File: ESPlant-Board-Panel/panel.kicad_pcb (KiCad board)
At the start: 4 copper layers, 70 x 116 mm, 150 parts, among them J1 Conn_01x05, U1 USB-C, U13 ESP32-C6-MINI-1-N4, U3 AHT20-F, U4 Tactile-Switch, U5 3.3V-Regulator, U6 Light sensor, U7 Tactile-Switch, U8 Slide-Switch, U9 Battery-Spring

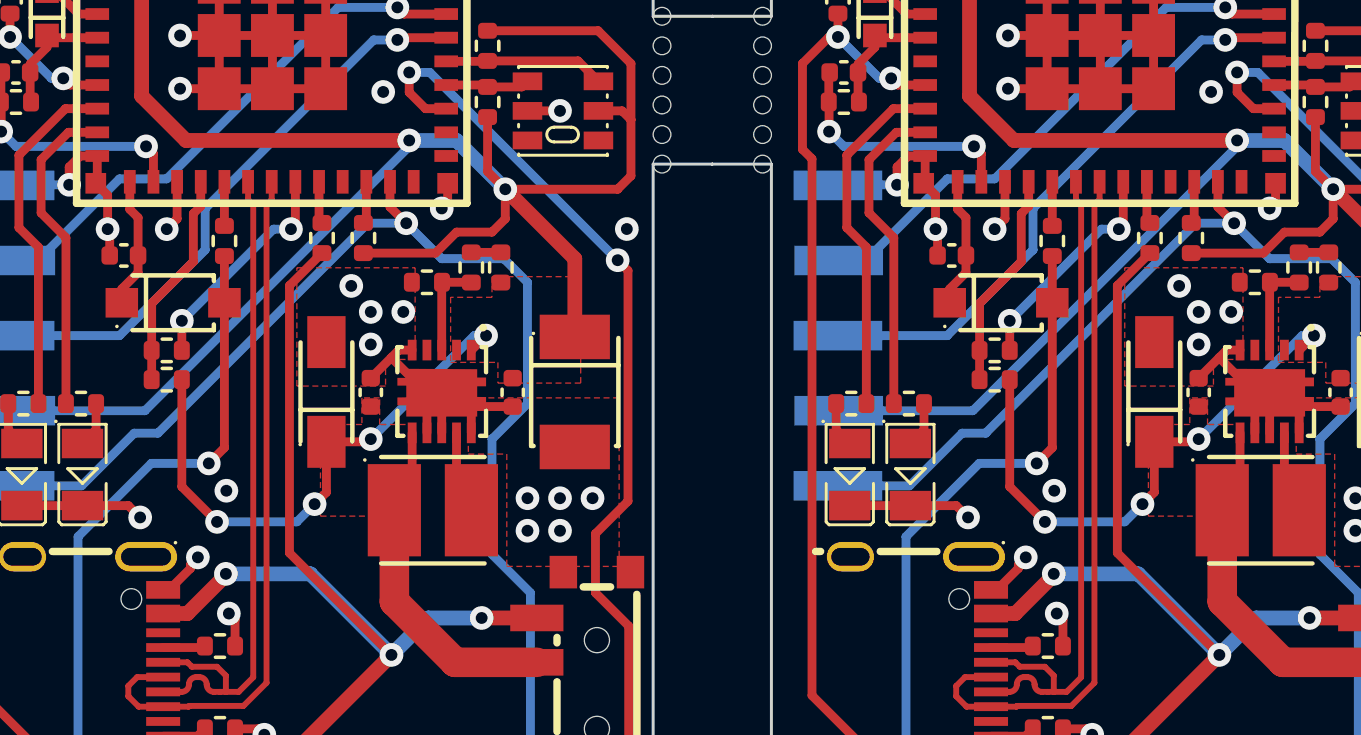
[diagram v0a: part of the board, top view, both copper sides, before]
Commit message: Panel: Add voltage divider for checking usb connection
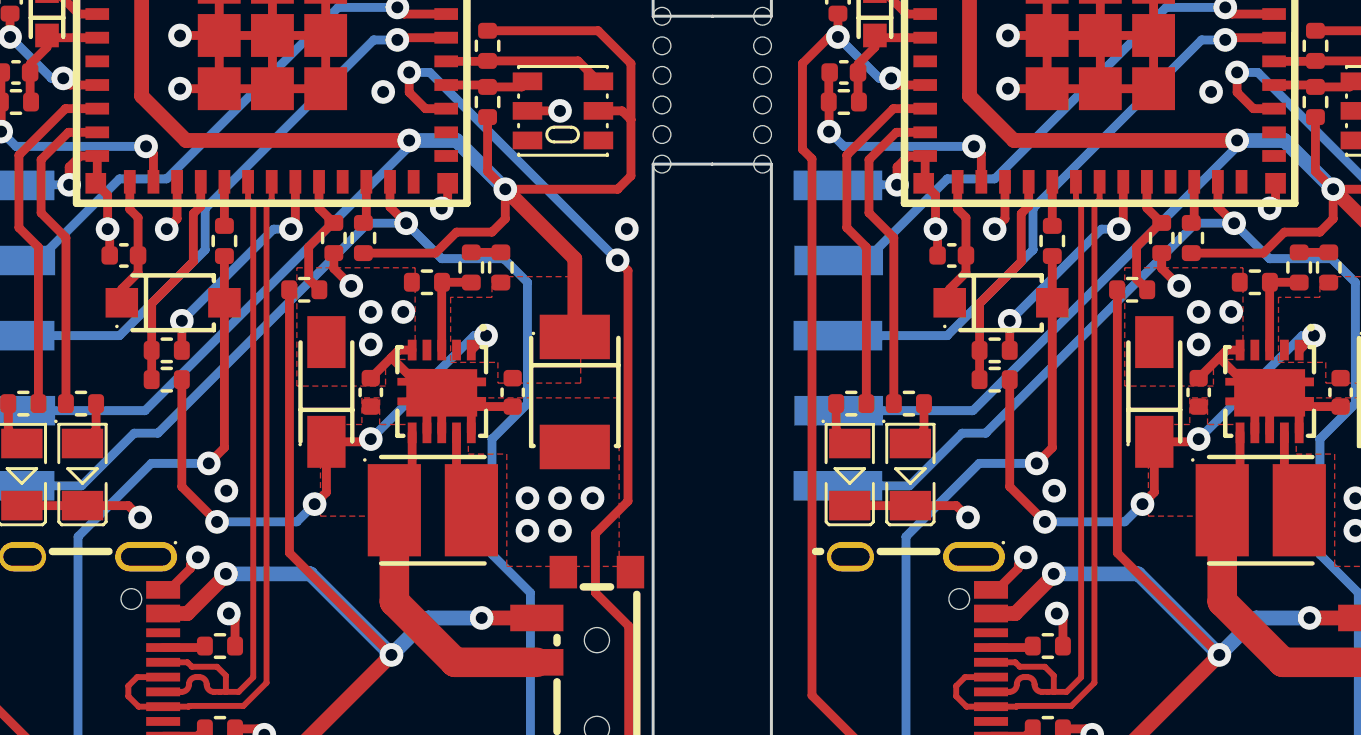
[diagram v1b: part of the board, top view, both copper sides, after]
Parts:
- removed the R7 at (239.8, 32.5)
- removed the R7 at (211.8, 32.5)
- added R17: 20k, Resistor_SMD:R_0402_1005Metric, F.Cu at (240.2, 32.5)
- added R17: 20k, Resistor_SMD:R_0402_1005Metric, F.Cu at (212.2, 32.5)
- added R7: 10k, Resistor_SMD:R_0402_1005Metric, F.Cu at (211.2, 34.2)
- added R7: 10k, Resistor_SMD:R_0402_1005Metric, F.Cu at (239.2, 34.2)
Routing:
- net Board_1-Net-(U13-IO15): track 1.43 -> 4.38 mm
- net Board_0-Net-(U13-IO15): track 1.43 -> 4.38 mm
- net Board_1-PWR_USB_VIN: track 39.7 -> 38.0 mm
- net Board_0-PWR_USB_VIN: track 39.7 -> 38.0 mm
- net Board_1-GND: track 219.9 -> 221.2 mm
- net Board_0-GND: track 219.9 -> 221.2 mm

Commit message: Board: Change AHT20-F to AHT20
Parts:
- U3 (x2): value AHT20-F -> AHT20

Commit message: Board: Add debug pin silkscreen
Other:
- board text added: "3V3"
- board text added: "GND"
- board text added: "IO9"
- board text added: "RX"
- board text added: "TX"

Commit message: Board: Add flower
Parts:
- added Flower1: Flower, CustomFootprints:Flower, B.Cu at (242.1, 46.1)
- added Flower1: Flower, CustomFootprints:Flower, B.Cu at (214.1, 46.1)

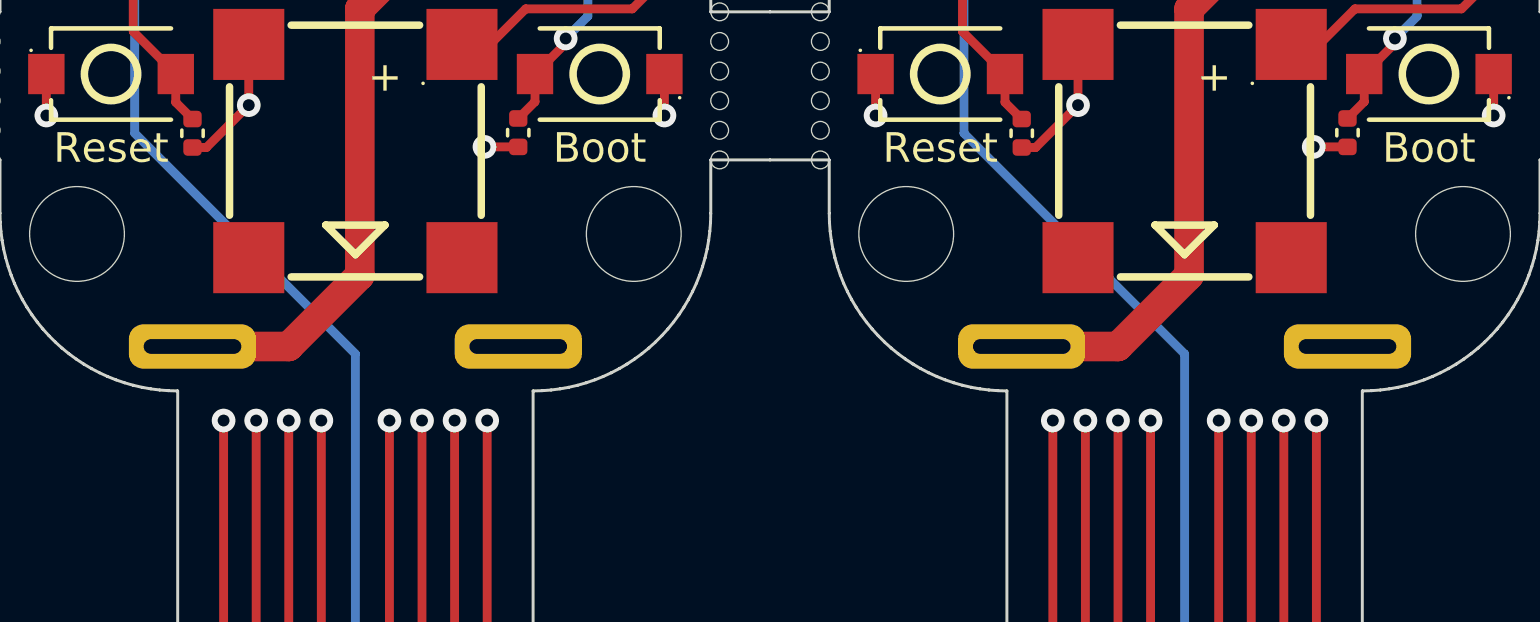
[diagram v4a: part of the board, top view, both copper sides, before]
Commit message: Switch battery polarity
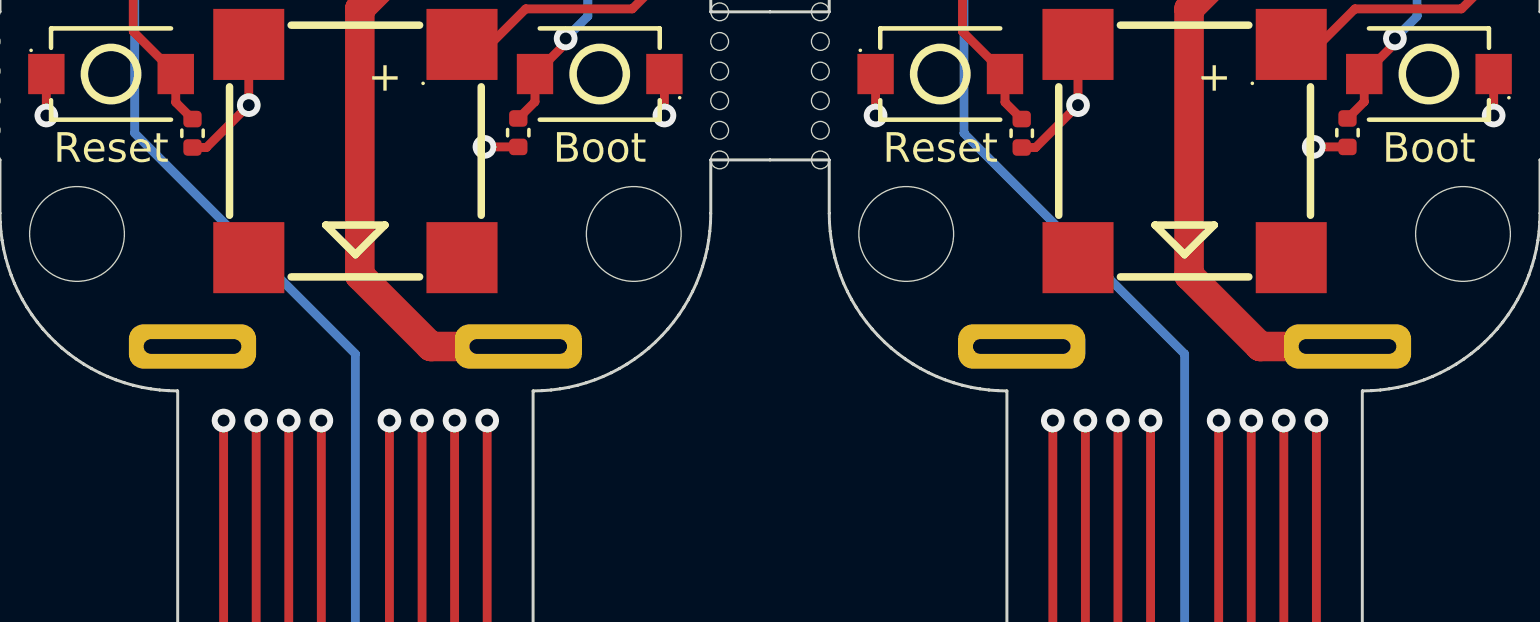
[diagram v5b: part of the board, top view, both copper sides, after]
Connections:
- U9 pad 1: Board_0-GND -> Board_0-PWR_BAT_VIN
- U9 pad 2: Board_0-PWR_BAT_VIN -> Board_0-GND
- U9 pad 1: Board_1-GND -> Board_1-PWR_BAT_VIN
- U9 pad 2: Board_1-PWR_BAT_VIN -> Board_1-GND
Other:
- board text added: "+"

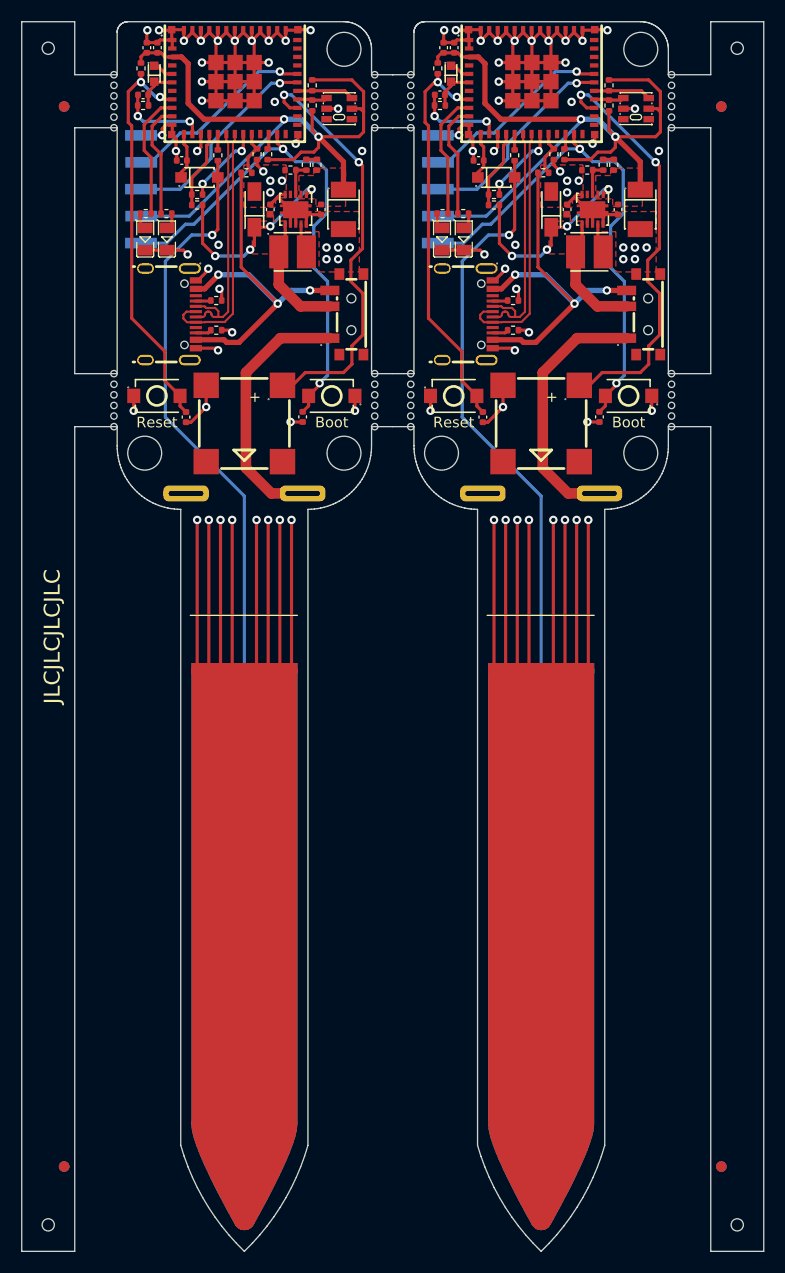
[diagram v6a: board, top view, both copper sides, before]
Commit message: Panel: Update panel
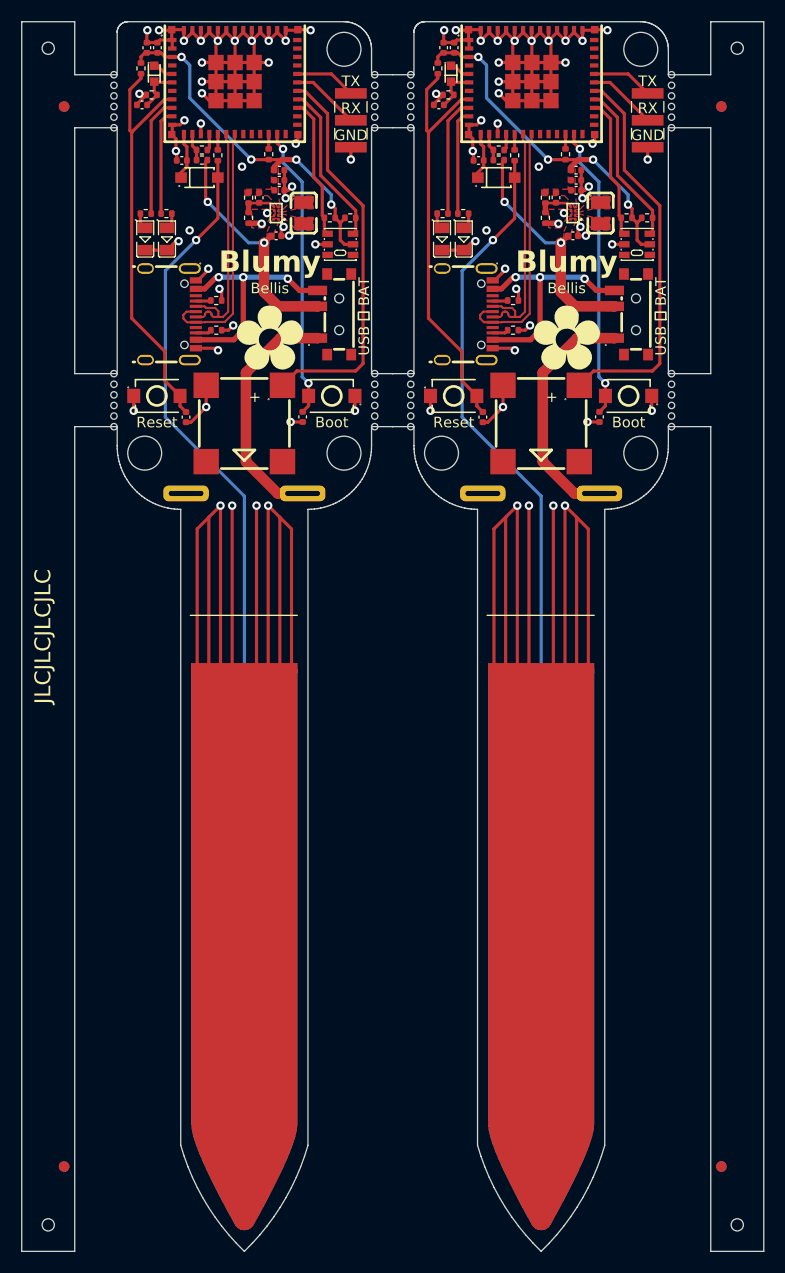
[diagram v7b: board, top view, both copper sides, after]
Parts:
- removed the C1 at (218.3, 37.7)
- removed the C1 at (246.3, 37.7)
- removed the C10 at (212.0, 37.7)
- removed the C10 at (240.0, 37.7)
- removed the C2 at (248.4, 37.7)
- removed the C2 at (220.4, 37.7)
- removed the C6 at (213.5, 37.7)
- removed the C6 at (241.5, 37.7)
- removed the C7 at (201.5, 26.9)
- removed the C7 at (229.5, 26.9)
- removed the D2 at (234.8, 34.7)
- removed the D2 at (206.8, 34.7)
- removed the Flower1 at (214.1, 46.1)
- removed the Flower1 at (242.1, 46.1)
- removed the J1 at (228.0, 35.8)
- removed the J1 at (200.0, 35.8)
- removed the L1 at (215.6, 41.7)
- removed the L1 at (243.6, 41.7)
- removed the R1 at (245.9, 33.5)
- removed the R1 at (217.9, 33.5)
- removed the R10 at (217.4, 27.9)
- removed the R10 at (245.4, 27.9)
- removed the R15 at (216.9, 33.5)
- removed the R15 at (244.9, 33.5)
- removed R16 (x2): 200k, Resistor_SMD:R_0402_1005Metric
- removed R17 (x2): 20k, Resistor_SMD:R_0402_1005Metric
- removed the R2 at (245.4, 26.0)
- removed the R2 at (217.4, 26.0)
- removed the R3 at (229.5, 27.9)
- removed the R3 at (201.5, 27.9)
- removed the R4 at (206.6, 37.3)
- removed the R4 at (234.6, 37.3)
- removed the R5 at (213.2, 32.5)
- removed the R5 at (241.2, 32.5)
- removed the R6 at (206.6, 36.3)
- removed the R6 at (234.6, 36.3)
- removed R7 (x2): 10k, Resistor_SMD:R_0402_1005Metric
- removed the U3 at (248.0, 28.2)
- removed the U3 at (220.0, 28.2)
- removed U5 (x2): 3.3V-Regulator, CustomFootprints:VSON-10_L3.0-W3.0-P0.50-BL-EP_TPS62410DRCR
- removed the U8 at (220.7, 47.6)
- removed the U8 at (248.7, 47.6)
- added C1: 10uF, Capacitor_SMD:C_0402_1005Metric, F.Cu at (214.0, 40.2)
- added C1: 10uF, Capacitor_SMD:C_0402_1005Metric, F.Cu at (242.0, 40.2)
- added C10: 10uF, Capacitor_SMD:C_0402_1005Metric, F.Cu at (242.3, 35.0)
- added C10: 10uF, Capacitor_SMD:C_0402_1005Metric, F.Cu at (214.3, 35.0)
- added C12: 10uF, Capacitor_SMD:C_0402_1005Metric, F.Cu at (242.3, 34.0)
- added C12: 10uF, Capacitor_SMD:C_0402_1005Metric, F.Cu at (214.3, 34.0)
- added C2: 10pF, Capacitor_SMD:C_0402_1005Metric, F.Cu at (212.4, 36.6)
- added C2: 10pF, Capacitor_SMD:C_0402_1005Metric, F.Cu at (240.4, 36.6)
- added C6: 10uF, Capacitor_SMD:C_0402_1005Metric, F.Cu at (214.3, 35.9)
- added C6: 10uF, Capacitor_SMD:C_0402_1005Metric, F.Cu at (242.3, 35.9)
- added C7: 10uF, Capacitor_SMD:C_0402_1005Metric, F.Cu at (201.4, 27.9)
- added C7: 10uF, Capacitor_SMD:C_0402_1005Metric, F.Cu at (229.4, 27.9)
- added D2: Switching-Diode, CustomFootprints:SOD-123F_L2.7-W1.6-LS3.8-RD, F.Cu at (206.8, 34.7)
- added D2: Switching-Diode, CustomFootprints:SOD-123F_L2.7-W1.6-LS3.8-RD, F.Cu at (234.8, 34.7)
- added Flower1: Flower, CustomFootprints:Flower, F.Cu at (213.4, 49.8)
- added Flower1: Flower, CustomFootprints:Flower, F.Cu at (241.4, 49.8)
- added J1: Conn_01x03, CustomFootprints:PinHeader_1x03_P2.54mm_Vertical_SMD, F.Cu at (221.1, 29.3)
- added J1: Conn_01x03, CustomFootprints:PinHeader_1x03_P2.54mm_Vertical_SMD, F.Cu at (249.1, 29.3)
- added L1: 1.5uH, CustomFootprints:L0806, F.Cu at (244.6, 38.0)
- added L1: 1.5uH, CustomFootprints:L0806, F.Cu at (216.6, 38.0)
- added R1: 287k, Resistor_SMD:R_0402_1005Metric, F.Cu at (239.4, 36.6)
- added R1: 287k, Resistor_SMD:R_0402_1005Metric, F.Cu at (211.4, 36.6)
- added R10: 5k1, Resistor_SMD:R_0402_1005Metric, F.Cu at (247.1, 38.5)
- added R10: 5k1, Resistor_SMD:R_0402_1005Metric, F.Cu at (219.1, 38.5)
- added R15: 51.1k, Resistor_SMD:R_0402_1005Metric, F.Cu at (211.4, 38.5)
- added R15: 51.1k, Resistor_SMD:R_0402_1005Metric, F.Cu at (239.4, 38.5)
- added R2: 5k1, Resistor_SMD:R_0402_1005Metric, F.Cu at (221.0, 38.5)
- added R2: 5k1, Resistor_SMD:R_0402_1005Metric, F.Cu at (249.0, 38.5)
- added R3: 100k, Resistor_SMD:R_0402_1005Metric, F.Cu at (230.3, 26.9)
- added R3: 100k, Resistor_SMD:R_0402_1005Metric, F.Cu at (202.3, 26.9)
- added R4: 5k1, Resistor_SMD:R_0402_1005Metric, F.Cu at (235.0, 33.0)
- added R4: 5k1, Resistor_SMD:R_0402_1005Metric, F.Cu at (207.0, 33.0)
- added R5: 10k, Resistor_SMD:R_0402_1005Metric, F.Cu at (241.3, 32.5)
- added R5: 10k, Resistor_SMD:R_0402_1005Metric, F.Cu at (213.3, 32.5)
- added R6: 2k, Resistor_SMD:R_0402_1005Metric, F.Cu at (207.0, 32.1)
- added R6: 2k, Resistor_SMD:R_0402_1005Metric, F.Cu at (235.0, 32.1)
- added REF1: TPS63036YFGR, CustomFootprints:DSBGA-8_L1.8-W1.1-R2-C4-P0.40-BR, F.Cu at (242.0, 38.0)
- added REF1: TPS63036YFGR, CustomFootprints:DSBGA-8_L1.8-W1.1-R2-C4-P0.40-BR, F.Cu at (214.0, 38.0)
- added U3: AHT20, CustomFootprints:SENSOR-SMD-6_AHT20, F.Cu at (220.1, 41.0)
- added U3: AHT20, CustomFootprints:SENSOR-SMD-6_AHT20, F.Cu at (248.1, 41.0)
- added U8: Slide-Switch, CustomFootprints:SW-SMD_MK-12C02-G025, F.Cu at (219.5, 47.6)
- added U8: Slide-Switch, CustomFootprints:SW-SMD_MK-12C02-G025, F.Cu at (247.5, 47.6)
- moved KiKit_MB_1_1 5.00 mm to (223.3, 53.2)
- moved KiKit_MB_1_6 5.00 mm to (223.3, 58.2)
- moved KiKit_MB_2_1 5.00 mm to (223.3, 25.0)
- moved KiKit_MB_2_6 5.00 mm to (223.3, 30.0)
- moved KiKit_MB_3_1 5.00 mm to (198.7, 58.2)
- moved KiKit_MB_3_6 5.00 mm to (198.7, 53.2)
- moved KiKit_MB_4_1 5.00 mm to (198.7, 30.0)
- moved KiKit_MB_4_6 5.00 mm to (198.7, 25.0)
- moved KiKit_MB_5_1 5.00 mm to (251.3, 53.2)
- moved KiKit_MB_5_6 5.00 mm to (251.3, 58.2)
- moved KiKit_MB_6_1 5.00 mm to (251.3, 25.0)
- moved KiKit_MB_6_6 5.00 mm to (251.3, 30.0)
- moved KiKit_MB_7_1 5.00 mm to (226.7, 58.2)
- moved KiKit_MB_7_6 5.00 mm to (226.7, 53.2)
- moved KiKit_MB_8_1 5.00 mm to (226.7, 30.0)
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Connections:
- U13 pad 13: Board_1-Light_Sensor_Select -> Board_1-ADC_Voltage_Measurement
- U13 pad 15: Board_1-ADC_Voltage_Measurement -> Board_1-Voltage_Measurement_Select
- U13 pad 19: Board_1-Voltage_Measurement_Select -> Board_1-unconnected-(U13-IO14-Pad19)
- U13 pad 20: Board_1-Net-(U13-IO15) -> Board_1-unconnected-(U13-IO15-Pad20)
- U13 pad 27: Board_1-Buzzer -> Board_1-TH_SDA
- U13 pad 28: Board_1-TH_SDA -> Board_1-TH_SCL
- U13 pad 29: Board_1-TH_SCL -> Board_1-Buzzer
- U13 pad 13: Board_0-Light_Sensor_Select -> Board_0-ADC_Voltage_Measurement
- U13 pad 15: Board_0-ADC_Voltage_Measurement -> Board_0-Voltage_Measurement_Select
- U13 pad 19: Board_0-Voltage_Measurement_Select -> Board_0-unconnected-(U13-IO14-Pad19)
- U13 pad 20: Board_0-Net-(U13-IO15) -> Board_0-unconnected-(U13-IO15-Pad20)
- U13 pad 27: Board_0-Buzzer -> Board_0-TH_SDA
- U13 pad 28: Board_0-TH_SDA -> Board_0-TH_SCL
- U13 pad 29: Board_0-TH_SCL -> Board_0-Buzzer
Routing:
- net Board_1-+3V3: track 70.1 -> 34.3 mm, vias 2 -> 4
- net Board_0-+3V3: track 70.1 -> 34.3 mm, vias 2 -> 4
- net Board_1-IO9: track 48.4 -> 27.7 mm
- net Board_0-IO9: track 48.4 -> 27.7 mm
- net Board_1-PWR_USB_VIN: track 38.0 -> 22.3 mm
- net Board_0-PWR_USB_VIN: track 38.0 -> 22.3 mm
- net Board_1-RX: track 19.7 -> 6.54 mm, vias 1 -> 0
- net Board_0-RX: track 19.7 -> 6.54 mm, vias 1 -> 0
- net Board_1-TX: track 18.4 -> 5.81 mm, vias 1 -> 0
- net Board_0-TX: track 18.4 -> 5.81 mm, vias 1 -> 0
- net Board_1-TH_SDA: track 2.86 -> 13.3 mm
- net Board_0-TH_SDA: track 2.86 -> 13.3 mm
- net Board_0-TH_SCL: track 5.44 -> 15.4 mm
- net Board_1-TH_SCL: track 5.44 -> 15.4 mm
- net Board_0-PWR_VIN: track 30.8 -> 22.2 mm, vias 4 -> 2
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- added copper zone on F.Cu, net Board_0-Net-(REF1-L1)
- added copper zone on F.Cu, net Board_0-Net-(REF1-L2)
- added copper zone on F.Cu, net Board_1-Net-(REF1-L1)
- added copper zone on F.Cu, net Board_1-Net-(REF1-L2)
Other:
- board text added: "Bellis"
- board text added: "USB 〡 BAT"
- board text removed: "+"
- board text removed: "3V3"
- board text removed: "Aconitum"
- board text removed: "IO9"
- board text removed: "USB〡BAT"
